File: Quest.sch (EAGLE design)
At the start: 45 parts, among them Q1 IRF740, Q2 IRF740, Q3 IRF740, Q4 IRF740

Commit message: Changes in pull-down values. Add PDF file with schema.
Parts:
- R27: value 150 -> 100k
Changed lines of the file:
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@@
 <part name="D1" library="diode" deviceset="1N4728" device=""/>
 <part name="D2" library="diode" deviceset="1N4728" device=""/>
-<part name="R27" library="rcl" deviceset="R-EU_" device="0309/10" value="150"/>
+<part name="R27" library="rcl" deviceset="R-EU_" device="0309/10" value="100k"/>
 <part name="GND22" library="supply1" deviceset="GND" device=""/>
 </parts>

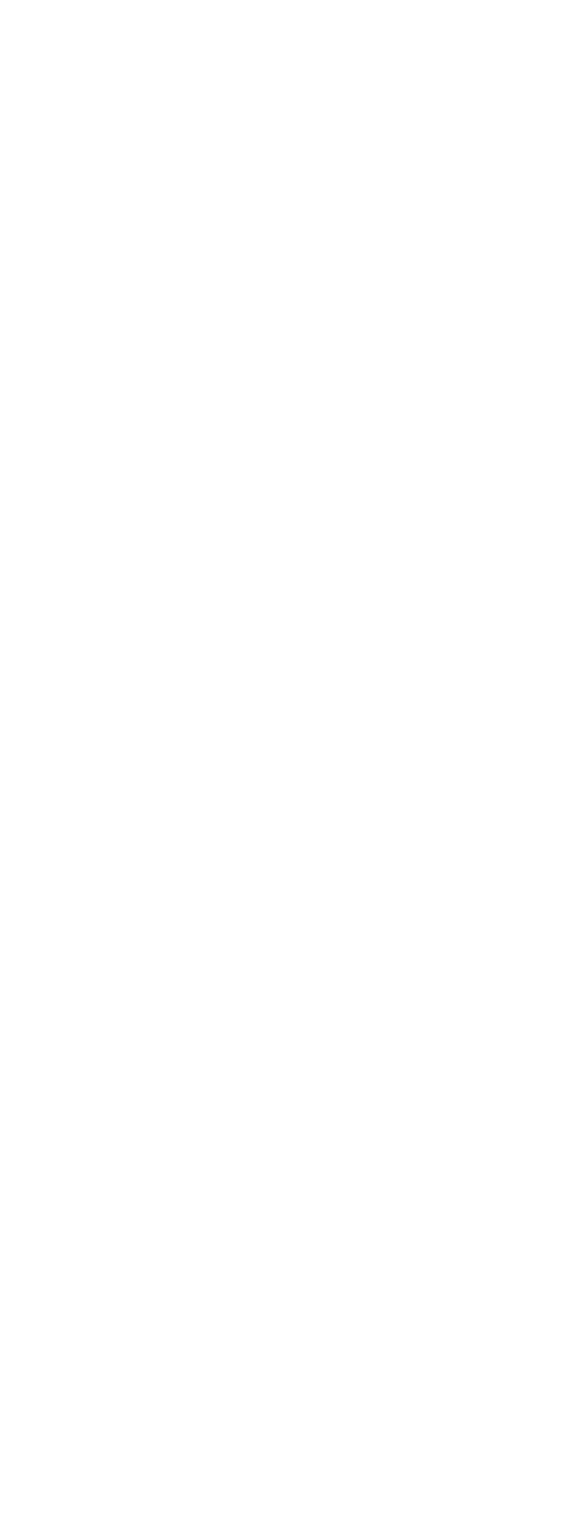
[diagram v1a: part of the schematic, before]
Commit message: Add LEDs and button for showing voltage into schema.
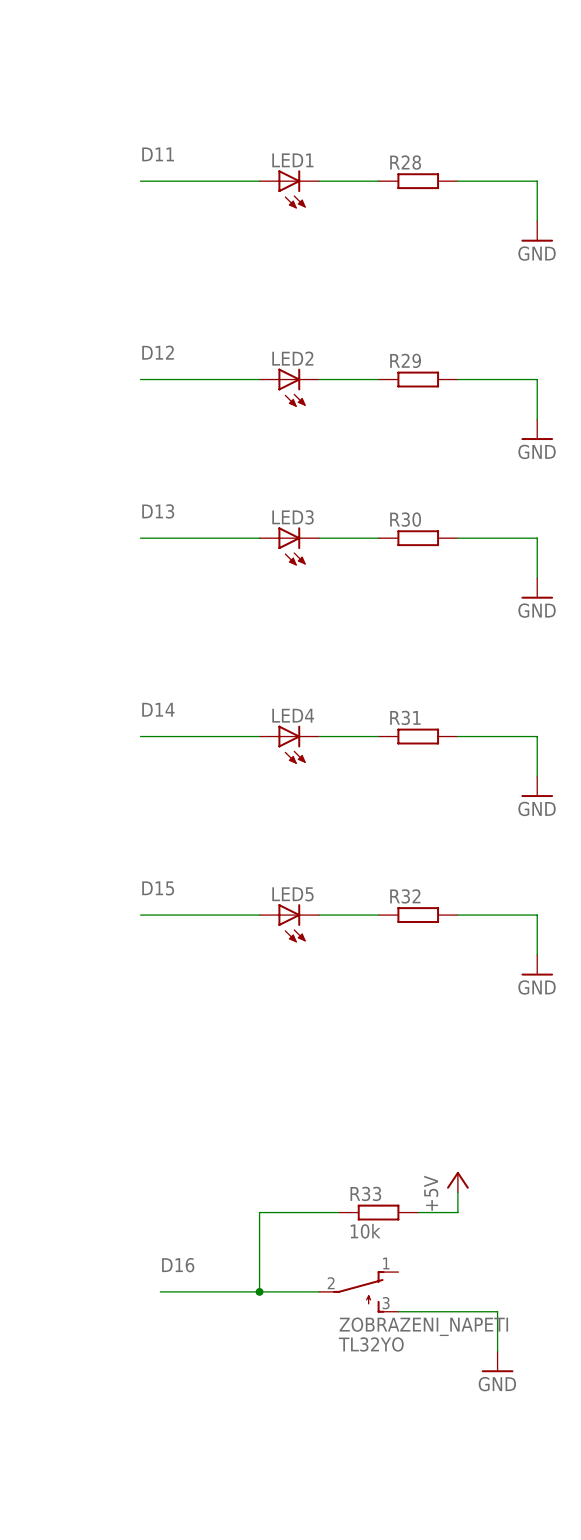
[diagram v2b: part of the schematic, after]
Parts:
- added LED1, LED2, LED3, LED4, LED5: (no value), led:LED5MM
- added R28, R29, R30, R31, R32: (no value), rcl:R-EU_0309/10
- added R33: 10k, rcl:R-EU_0309/10
- added ZOBRAZENI_NAPETI: TL32YO, switch:TL32YO
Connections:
- new net D11: LED1.A
- new net D12: LED2.A
- new net D13: LED3.A
- new net D14: LED4.A
- new net D15: LED5.A
- new net D16: R33.1, ZOBRAZENI_NAPETI.P
- new net N$10: LED2.C, R29.1
- new net N$12: LED1.C, R28.1
- new net N$13: LED3.C, R30.1
- new net N$14: LED4.C, R31.1
- new net N$15: LED5.C, R32.1
- net +5V: now also R33.2
- net GND: now also R28.2, R29.2, R30.2, R31.2, R32.2, ZOBRAZENI_NAPETI.S
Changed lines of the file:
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@@
 <part name="R27" library="rcl" deviceset="R-EU_" device="0309/10" value="100k"/>
 <part name="GND22" library="supply1" deviceset="GND" device=""/>
+<part name="LED1" library="led" deviceset="LED" device="5MM"/>
+<part name="GND23" library="supply1" deviceset="GND" device=""/>
+<part name="R28" library="rcl" deviceset="R-EU_" device="0309/10"/>
+<part name="LED2" library="led" deviceset="LED" device="5MM"/>
+<part name="GND24" library="supply1" deviceset="GND" device=""/>
+<part name="R29" library="rcl" deviceset="R-EU_" device="0309/10"/>
+<part name="LED3" library="led" deviceset="LED" device="5MM"/>
+<part name="GND25" library="supply1" deviceset="GND" device=""/>
+<part name="R30" library="rcl" deviceset="R-EU_" device="0309/10"/>
+<part name="LED4" library="led" deviceset="LED" device="5MM"/>
+<part name="GND26" library="supply1" deviceset="GND" device=""/>
+<part name="R31" library="rcl" deviceset="R-EU_" device="0309/10"/>
+<part name="LED5" library="led" deviceset="LED" device="5MM"/>
+<part name="GND27" library="supply1" deviceset="GND" device=""/>
+<part name="R32" library="rcl" deviceset="R-EU_" device="0309/10"/>
+<part name="ZOBRAZENI_NAPETI" library="switch" deviceset="TL32YO" device=""/>
+<part name="GND28" library="supply1" deviceset="GND" device=""/>
+<part name="R33" library="rcl" deviceset="R-EU_" device="0309/10" value="10k"/>
+<part name="P+5" library="supply1" deviceset="+5V" device=""/>
 </parts>
 <sheets>
@@
 <instance part="R27" gate="G$1" x="10.16" y="147.32" rot="R90"/>
 <instance part="GND22" gate="1" x="10.16" y="134.62"/>
+<instance part="LED1" gate="G$1" x="350.52" y="160.02" rot="R90"/>
+<instance part="GND23" gate="1" x="383.54" y="152.4"/>
+<instance part="R28" gate="G$1" x="368.3" y="160.02"/>
+<instance part="LED2" gate="G$1" x="350.52" y="134.62" rot="R90"/>
+<instance part="GND24" gate="1" x="383.54" y="127"/>
+<instance part="R29" gate="G$1" x="368.3" y="134.62"/>
+<instance part="LED3" gate="G$1" x="350.52" y="114.3" rot="R90"/>
+<instance part="GND25" gate="1" x="383.54" y="106.68"/>
+<instance part="R30" gate="G$1" x="368.3" y="114.3"/>
+<instance part="LED4" gate="G$1" x="350.52" y="88.9" rot="R90"/>
+<instance part="GND26" gate="1" x="383.54" y="81.28"/>
+<instance part="R31" gate="G$1" x="368.3" y="88.9"/>
+<instance part="LED5" gate="G$1" x="350.52" y="66.04" rot="R90"/>
+<instance part="GND27" gate="1" x="383.54" y="58.42"/>
+<instance part="R32" gate="G$1" x="368.3" y="66.04"/>
+<instance part="ZOBRAZENI_NAPETI" gate="BEF1" x="360.68" y="17.78" rot="R270"/>
+<instance part="GND28" gate="1" x="378.46" y="7.62"/>
+<instance part="R33" gate="G$1" x="363.22" y="27.94"/>
+<instance part="P+5" gate="1" x="373.38" y="33.02"/>
 </instances>
 <busses>
@@
 <pinref part="R27" gate="G$1" pin="1"/>
 <wire x1="10.16" y1="137.16" x2="10.16" y2="142.24" width="0.1524" layer="91"/>
+</segment>
+<segment>
+<pinref part="R28" gate="G$1" pin="2"/>
+<wire x1="373.38" y1="160.02" x2="383.54" y2="160.02" width="0.1524" layer="91"/>
+<pinref part="GND23" gate="1" pin="GND"/>
+<wire x1="383.54" y1="160.02" x2="383.54" y2="154.94" width="0.1524" layer="91"/>
+</segment>
+<segment>
+<pinref part="R29" gate="G$1" pin="2"/>
+<wire x1="373.38" y1="134.62" x2="383.54" y2="134.62" width="0.1524" layer="91"/>
+<pinref part="GND24" gate="1" pin="GND"/>
+<wire x1="383.54" y1="134.62" x2="383.54" y2="129.54" width="0.1524" layer="91"/>
+</segment>
+<segment>
+<pinref part="R30" gate="G$1" pin="2"/>
+<wire x1="373.38" y1="114.3" x2="383.54" y2="114.3" width="0.1524" layer="91"/>
+<pinref part="GND25" gate="1" pin="GND"/>
+<wire x1="383.54" y1="114.3" x2="383.54" y2="109.22" width="0.1524" layer="91"/>
+</segment>
+<segment>
+<pinref part="R31" gate="G$1" pin="2"/>
+<wire x1="373.38" y1="88.9" x2="383.54" y2="88.9" width="0.1524" layer="91"/>
+<pinref part="GND26" gate="1" pin="GND"/>
+<wire x1="383.54" y1="88.9" x2="383.54" y2="83.82" width="0.1524" layer="91"/>
+</segment>
+<segment>
+<pinref part="R32" gate="G$1" pin="2"/>
+<wire x1="373.38" y1="66.04" x2="383.54" y2="66.04" width="0.1524" layer="91"/>
+<pinref part="GND27" gate="1" pin="GND"/>
+<wire x1="383.54" y1="66.04" x2="383.54" y2="60.96" width="0.1524" layer="91"/>
+</segment>
+<segment>
+<pinref part="ZOBRAZENI_NAPETI" gate="BEF1" pin="S"/>
+<pinref part="GND28" gate="1" pin="GND"/>
+<wire x1="365.76" y1="15.24" x2="378.46" y2="15.24" width="0.1524" layer="91"/>
+<wire x1="378.46" y1="15.24" x2="378.46" y2="10.16" width="0.1524" layer="91"/>
 </segment>
 </net>
@@
 <wire x1="175.26" y1="152.4" x2="175.26" y2="157.48" width="0.1524" layer="91"/>
 </segment>
+<segment>
+<pinref part="R33" gate="G$1" pin="2"/>
+<pinref part="P+5" gate="1" pin="+5V"/>
+<wire x1="368.3" y1="27.94" x2="373.38" y2="27.94" width="0.1524" layer="91"/>
+<wire x1="373.38" y1="27.94" x2="373.38" y2="30.48" width="0.1524" layer="91"/>
+</segment>
 </net>
 <net name="VCC" class="0">
@@
 </segment>
 </net>
+<net name="N$12" class="0">
+<segment>
+<pinref part="R28" gate="G$1" pin="1"/>
+<pinref part="LED1" gate="G$1" pin="C"/>
+<wire x1="363.22" y1="160.02" x2="355.6" y2="160.02" width="0.1524" layer="91"/>
+</segment>
+</net>
+<net name="D11" class="0">
+<segment>
+<pinref part="LED1" gate="G$1" pin="A"/>
+<wire x1="347.98" y1="160.02" x2="332.74" y2="160.02" width="0.1524" layer="91"/>
+<label x="332.74" y="162.56" size="1.778" layer="95"/>
+</segment>
+</net>
+<net name="N$10" class="0">
+<segment>
+<pinref part="R29" gate="G$1" pin="1"/>
+<pinref part="LED2" gate="G$1" pin="C"/>
+<wire x1="363.22" y1="134.62" x2="355.6" y2="134.62" width="0.1524" layer="91"/>
+</segment>
+</net>
+<net name="N$13" class="0">
+<segment>
+<pinref part="R30" gate="G$1" pin="1"/>
+<pinref part="LED3" gate="G$1" pin="C"/>
+<wire x1="363.22" y1="114.3" x2="355.6" y2="114.3" width="0.1524" layer="91"/>
+</segment>
+</net>
+<net name="N$14" class="0">
+<segment>
+<pinref part="R31" gate="G$1" pin="1"/>
+<pinref part="LED4" gate="G$1" pin="C"/>
+<wire x1="363.22" y1="88.9" x2="355.6" y2="88.9" width="0.1524" layer="91"/>
+</segment>
+</net>
+<net name="N$15" class="0">
+<segment>
+<pinref part="R32" gate="G$1" pin="1"/>
+<pinref part="LED5" gate="G$1" pin="C"/>
+<wire x1="363.22" y1="66.04" x2="355.6" y2="66.04" width="0.1524" layer="91"/>
+</segment>
+</net>
+<net name="D12" class="0">
+<segment>
+<pinref part="LED2" gate="G$1" pin="A"/>
+<wire x1="347.98" y1="134.62" x2="332.74" y2="134.62" width="0.1524" layer="91"/>
+<label x="332.74" y="137.16" size="1.778" layer="95"/>
+</segment>
+</net>
+<net name="D13" class="0">
+<segment>
+<pinref part="LED3" gate="G$1" pin="A"/>
+<wire x1="347.98" y1="114.3" x2="332.74" y2="114.3" width="0.1524" layer="91"/>
+<label x="332.74" y="116.84" size="1.778" layer="95"/>
+</segment>
+</net>
+<net name="D14" class="0">
+<segment>
+<pinref part="LED4" gate="G$1" pin="A"/>
+<wire x1="347.98" y1="88.9" x2="332.74" y2="88.9" width="0.1524" layer="91"/>
+<label x="332.74" y="91.44" size="1.778" layer="95"/>
+</segment>
+</net>
+<net name="D15" class="0">
+<segment>
+<pinref part="LED5" gate="G$1" pin="A"/>
+<wire x1="347.98" y1="66.04" x2="332.74" y2="66.04" width="0.1524" layer="91"/>
+<label x="332.74" y="68.58" size="1.778" layer="95"/>
+</segment>
+</net>
+<net name="D16" class="0">
+<segment>
+<pinref part="ZOBRAZENI_NAPETI" gate="BEF1" pin="P"/>
+<wire x1="355.6" y1="17.78" x2="347.98" y2="17.78" width="0.1524" layer="91"/>
+<label x="335.28" y="20.32" size="1.778" layer="95"/>
+<pinref part="R33" gate="G$1" pin="1"/>
+<wire x1="347.98" y1="17.78" x2="335.28" y2="17.78" width="0.1524" layer="91"/>
+<wire x1="358.14" y1="27.94" x2="347.98" y2="27.94" width="0.1524" layer="91"/>
+<wire x1="347.98" y1="27.94" x2="347.98" y2="17.78" width="0.1524" layer="91"/>
+<junction x="347.98" y="17.78"/>
+</segment>
+</net>

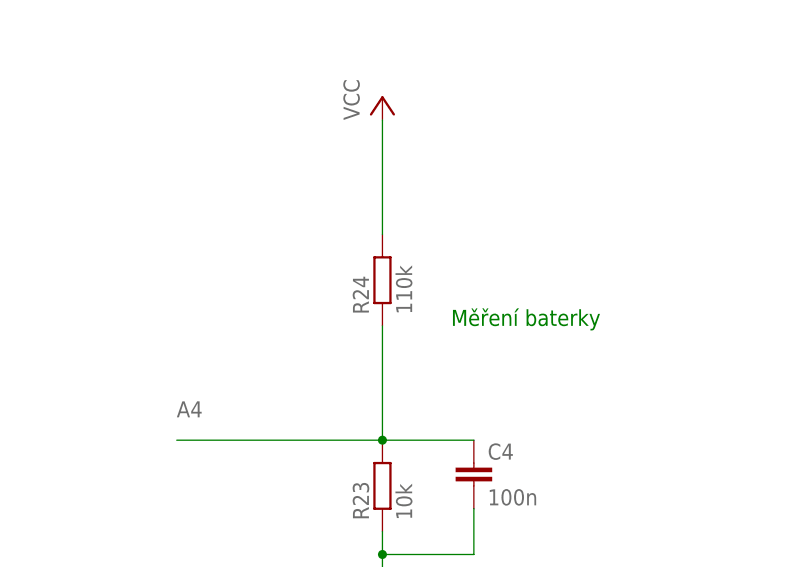
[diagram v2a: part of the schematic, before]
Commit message: Real voltage divider values in schema.
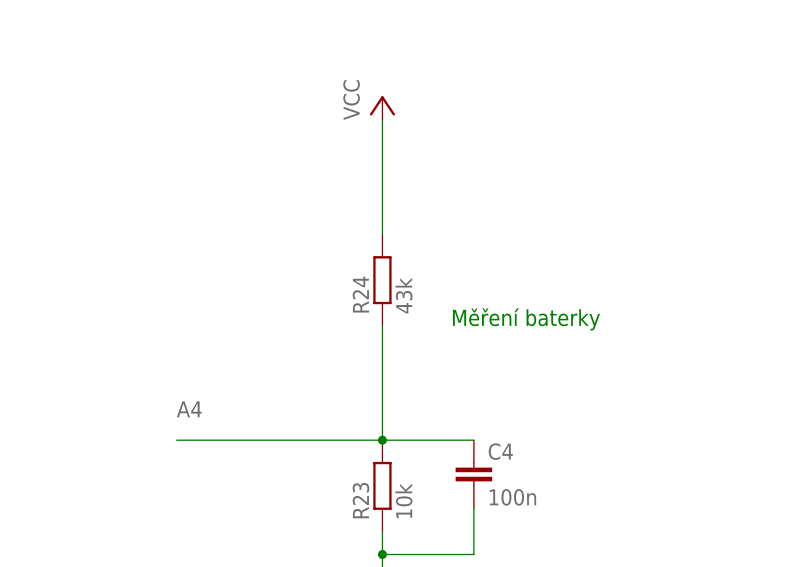
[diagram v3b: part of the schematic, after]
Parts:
- R24: value 110k -> 43k
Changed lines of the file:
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@@
 <part name="P+8" library="supply1" deviceset="+5V" device=""/>
 <part name="R23" library="rcl" deviceset="R-EU_" device="0309/10" value="10k"/>
-<part name="R24" library="rcl" deviceset="R-EU_" device="0309/10" value="110k"/>
+<part name="R24" library="rcl" deviceset="R-EU_" device="0309/10" value="43k"/>
 <part name="C4" library="rcl" deviceset="C-EU" device="050-024X044" value="100n"/>
 <part name="GND19" library="supply1" deviceset="GND" device=""/>
